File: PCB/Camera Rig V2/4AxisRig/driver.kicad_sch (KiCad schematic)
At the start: 24 parts, among them J3 Motor Connector, U5 TMC2209-LA

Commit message: PCB V2 first draft
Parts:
- removed R27: 220m, Resistor_SMD:R_0603_1608Metric_Pad0.98x0.95mm_HandSolder, symbol Device:R_US
- added R35: 0.68, Resistor_SMD:R_1206_3216Metric_Pad1.30x1.75mm_HandSolder, symbol Device:R_US
- C29: value 100n 16V -> 100nF 16V; footprint (none) -> Capacitor_SMD:C_0603_1608Metric_Pad1.08x0.95mm_HandSolder
- C30, C31, C32, C33, C35, C36, C37, C38: footprint (none) -> Capacitor_SMD:C_0603_1608Metric_Pad1.08x0.95mm_HandSolder
- C34: footprint (none) -> 865080545012:WCAP-ASLI_6.3X7.7_DXL_; Link (none) -> https://www.digikey.com/en/products/detail/w%C3%BCrth-elekt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
- R28: value 220m -> 0.68; footprint Resistor_SMD:R_0603_1608Metric_Pad0.98x0.95mm_HandSolder -> Resistor_SMD:R_1206_3216Metric_Pad1.30x1.75mm_HandSolder
- RV1, RV2: footprint Resistor_SMD:R_0603_1608Metric_Pad0.98x0.95mm_HandSolder -> Resistor_SMD:R_1206_3216Metric_Pad1.30x1.75mm_HandSolder
- U5: Unique FP y -> (none)
- renumbered R23 to R24, R24 to R25, R25 to R26, R26 to R27
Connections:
- net GND: now also R35.1
- net OA1: now also FB2.1; no longer FB1.1
- net OA2: now also FB1.1; no longer FB2.1
- net VS: now also C32.2, C33.2, C34.1
- net at U5.27 (BRB): now also R35.2
- new net: C29.2, U5.6 (VCP)
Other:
- note added: "UART Address Resistors"
- note removed: "Optional MIcrostep/Address Resistors If using UART, set address using pull up/down, leave extra pads open Else, use to set microstepping, leave extra pads open"
- moved on the sheet: C29, C32, C33, C34

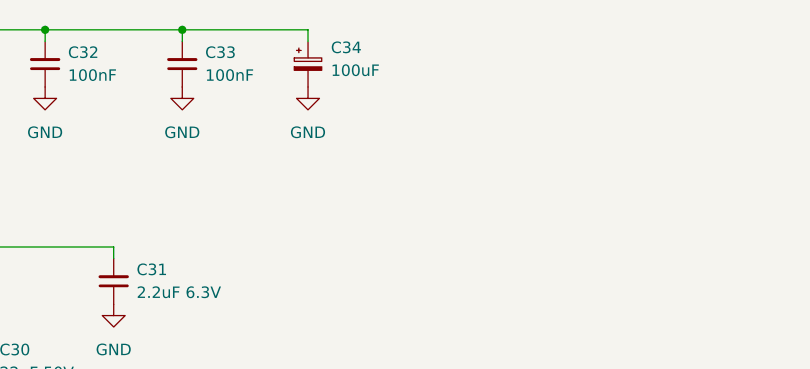
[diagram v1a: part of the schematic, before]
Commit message: REplaced bulk caps w low esr ceramics
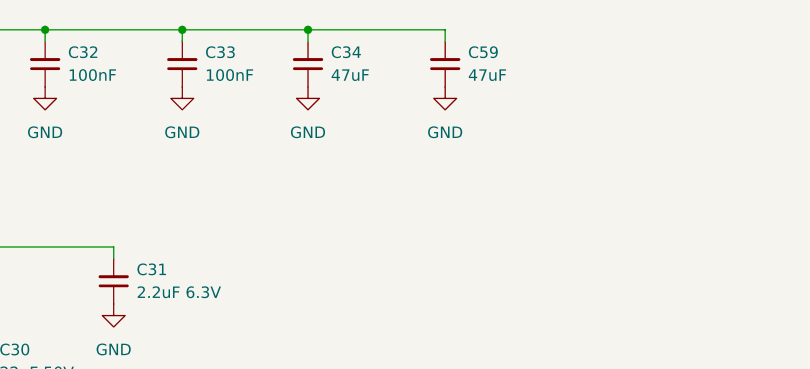
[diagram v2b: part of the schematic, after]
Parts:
- removed C34: 100uF, 865080545012:WCAP-ASLI_6.3X7.7_DXL_, symbol Device:C_Polarized_Small
- added C34, C59: 47uF, Capacitor_SMD:C_1210_3225Metric_Pad1.33x2.70mm_HandSolder, symbol Device:C_Small
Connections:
- net GND: now also C34.1, C59.1
- net VS: now also C34.2, C59.2

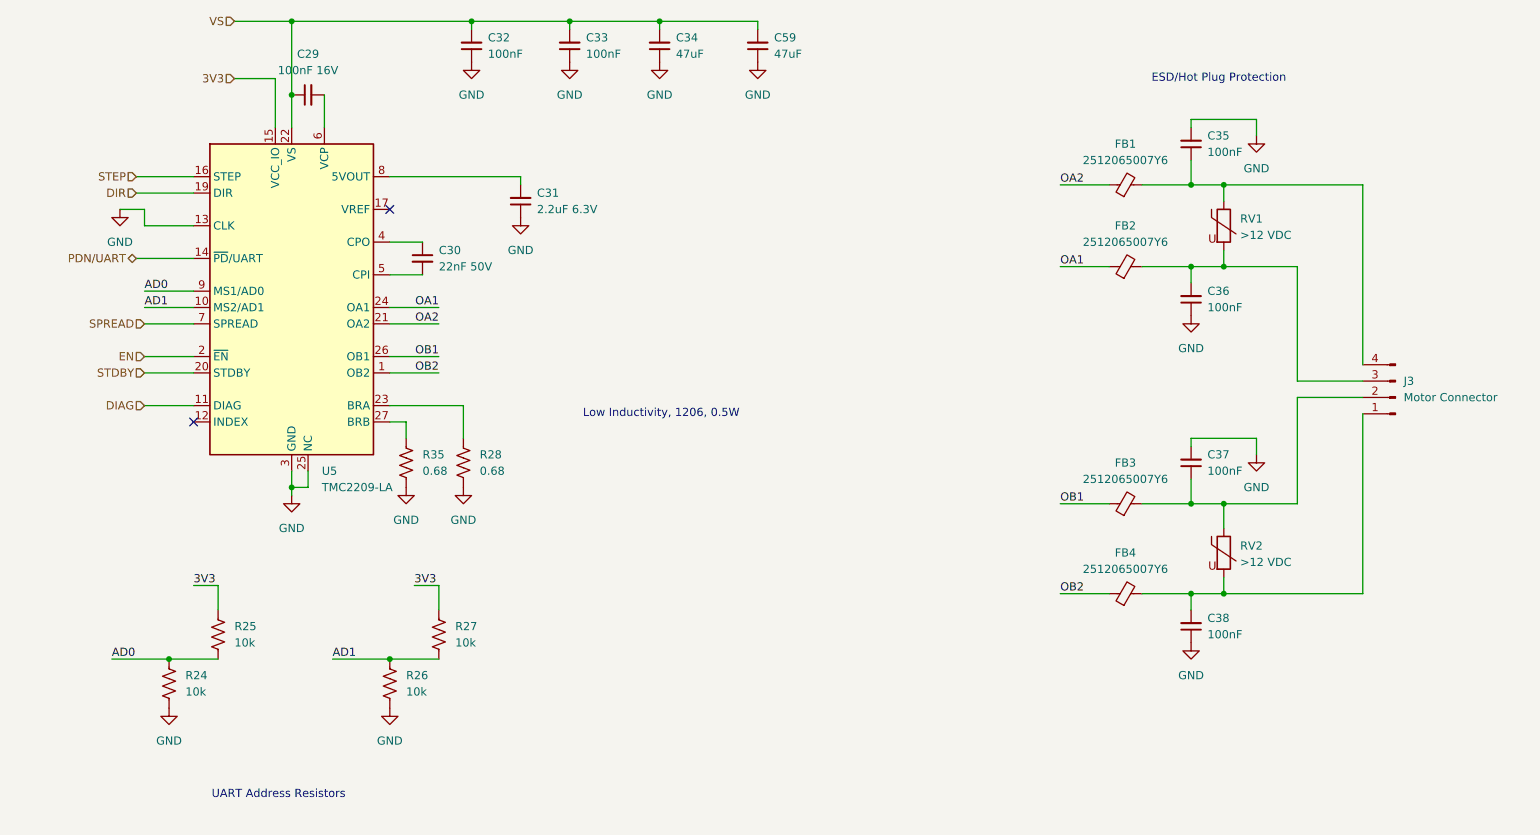
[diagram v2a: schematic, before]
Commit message: Netclass Improvements
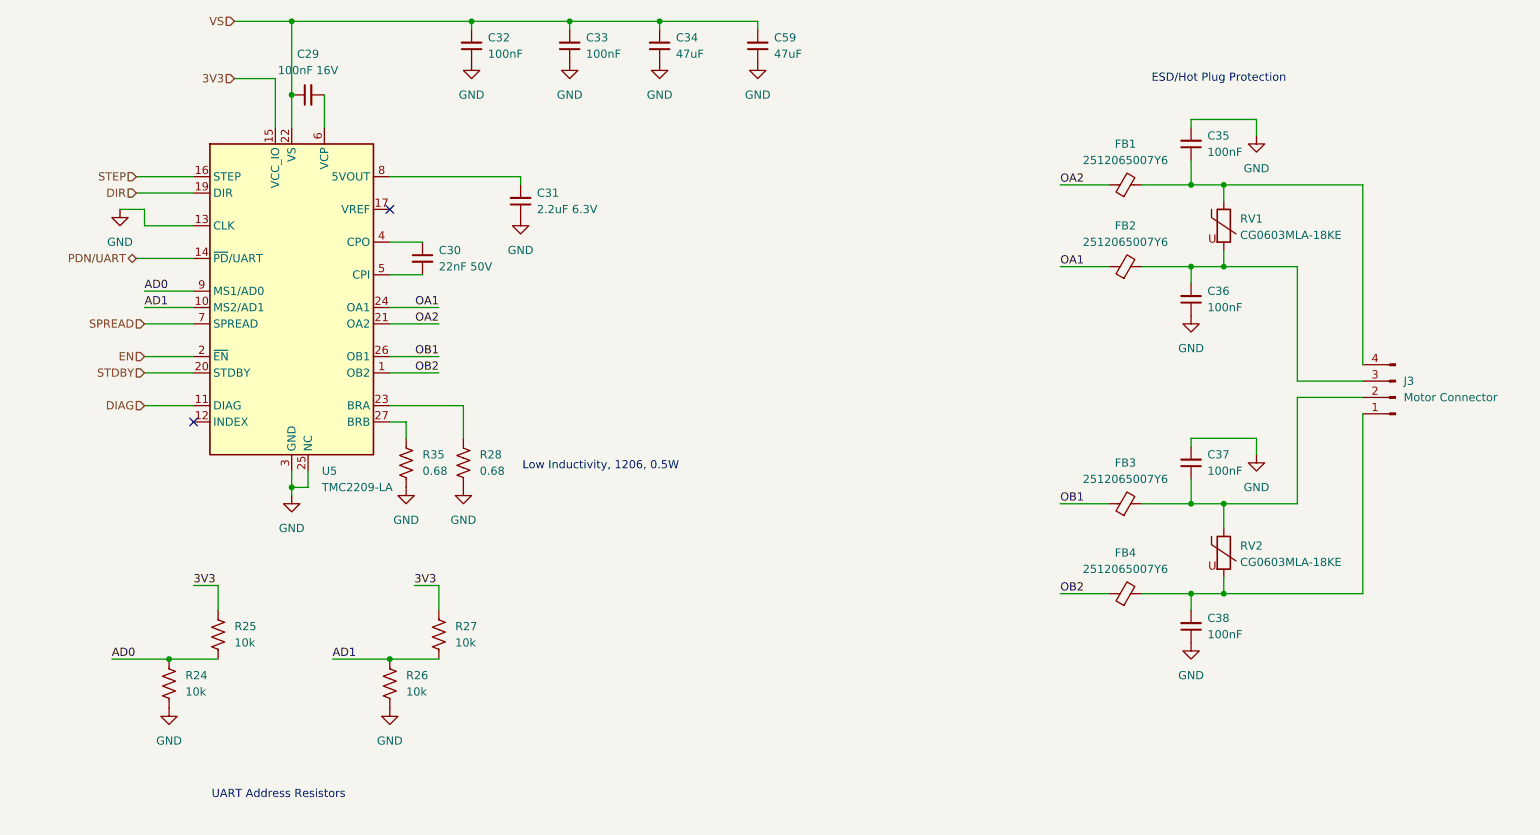
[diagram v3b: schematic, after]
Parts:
- RV1, RV2: value >12 VDC -> CG0603MLA-18KE
